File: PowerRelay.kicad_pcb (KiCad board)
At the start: 2 copper layers, 100 x 100 mm, 29 parts, among them J1 Screw_Terminal_01x03, J2 Conn_01x20_Female, J3 Conn_01x20_Female, J4 Conn_01x02_Female, J5 Screw_Terminal_01x03, J6 Screw_Terminal_01x03, J7 Conn_01x02_Female, J8 AudioJack4, K1 G5LE-1A4_DC3, K2 G5LE-1A4_DC3, Q1 2N7000, Q2 2N7000

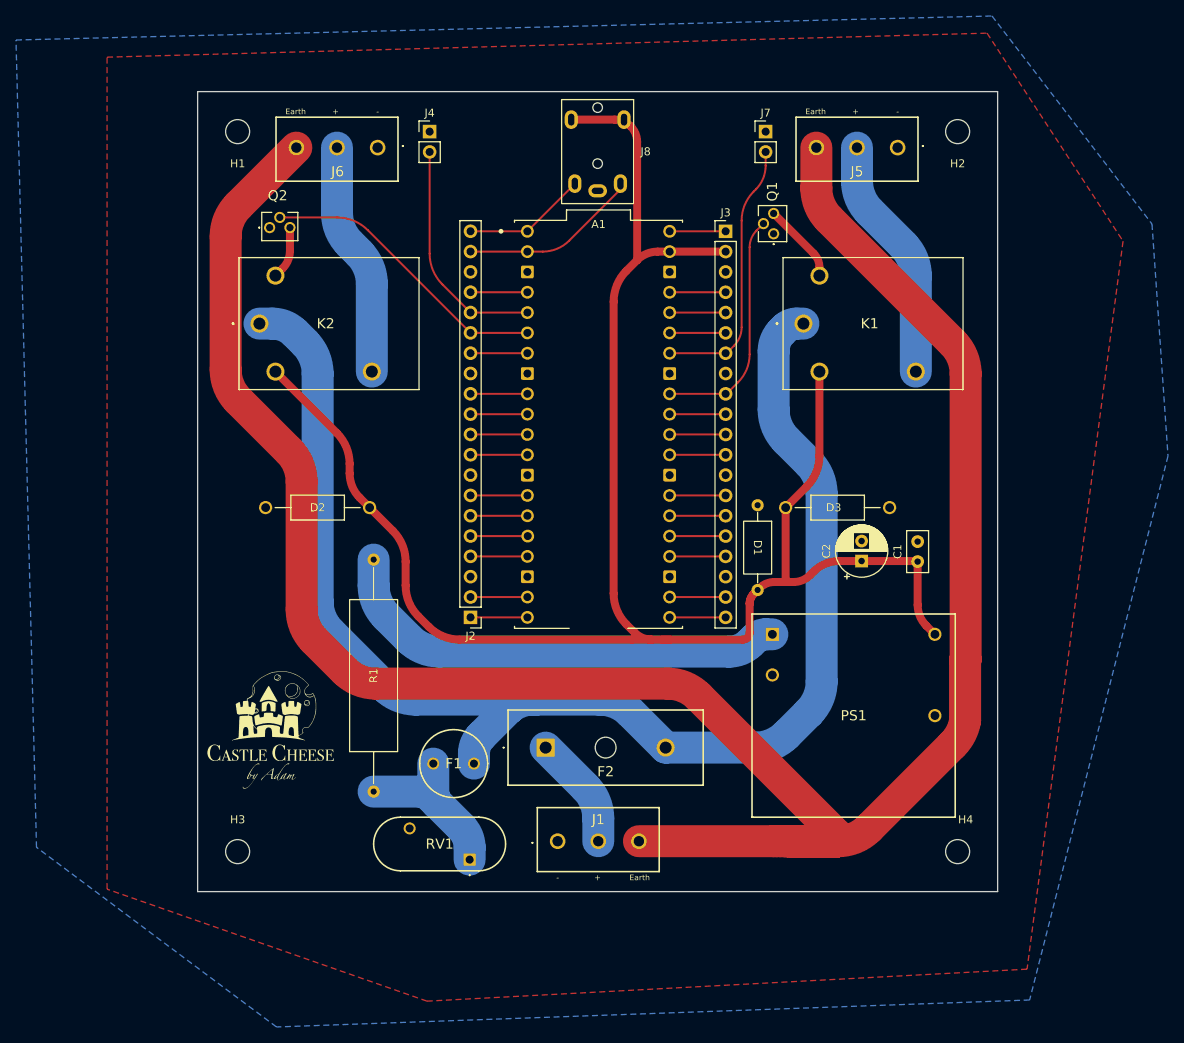
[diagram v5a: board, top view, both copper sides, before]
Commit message: add cutout for plugs to sit
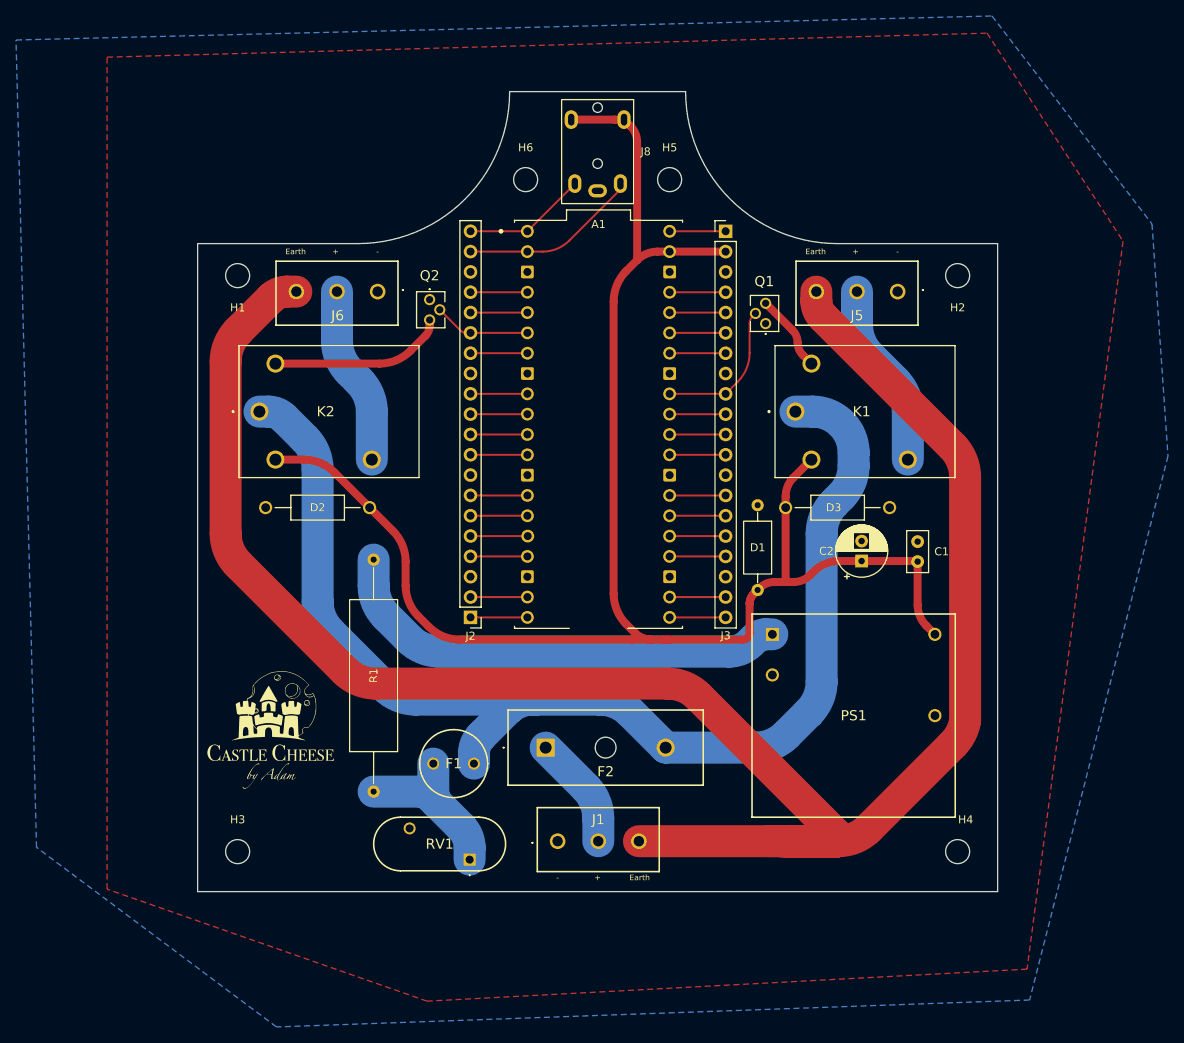
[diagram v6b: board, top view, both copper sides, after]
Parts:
- removed J4, J7: Conn_01x02_Female, Connector_PinHeader_2.54mm:PinHeader_1x02_P2.54mm_Vertical
- added H5: MountingHole, MountingHole:MountingHole_3mm, F.Cu at (109.0, 61.0)
- added H6: MountingHole, MountingHole:MountingHole_3mm, F.Cu at (91.0, 61.0)
- moved Q2 21.9 mm to (79.0, 76.0), turned to -90 degrees
- moved H1 18.0 mm to (55.0, 73.0)
- moved H2 18.0 mm to (145.0, 73.0)
- moved J5 18.0 mm to (137.5, 75.0)
- moved J6 18.0 mm to (72.5, 75.0)
- moved Q1 11.3 mm to (121.0, 79.0)
- moved K1 11.0 mm to (133.0, 90.0)
- moved K2 11.0 mm to (66.0, 90.0)
- moved G*** 7.00 mm to (117.1, 129.9)
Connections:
- net Cooling Switch renamed Net-(A1-Pad5)
- net Heating SW renamed Net-(A1-Pad34)
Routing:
- net Earth: track 270.9 -> 236.7 mm
- net Net-(A1-Pad34): track 33.5 -> 6.94 mm
- net Cooling: track 36.7 -> 12.1 mm
- net Net-(A1-Pad5): track 29.0 -> 7.11 mm
- net VAC: track 177.6 -> 157.0 mm
- net +3V3: track 235.0 -> 216.3 mm
- net Net-(K2-Pad5): track 6.60 -> 22.0 mm
- net Heating: track 29.9 -> 18.4 mm
- net Net-(J5-Pad2): track 30.5 -> 23.1 mm
- net Net-(J6-Pad2): track 29.3 -> 22.3 mm
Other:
- outline, holes or cut-outs redrawn
